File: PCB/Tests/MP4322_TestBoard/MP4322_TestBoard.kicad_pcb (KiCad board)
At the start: 2 copper layers, 30 parts, among them J1 Conn_01x02, J2 Conn_01x02, U7 MP4322GDE-P

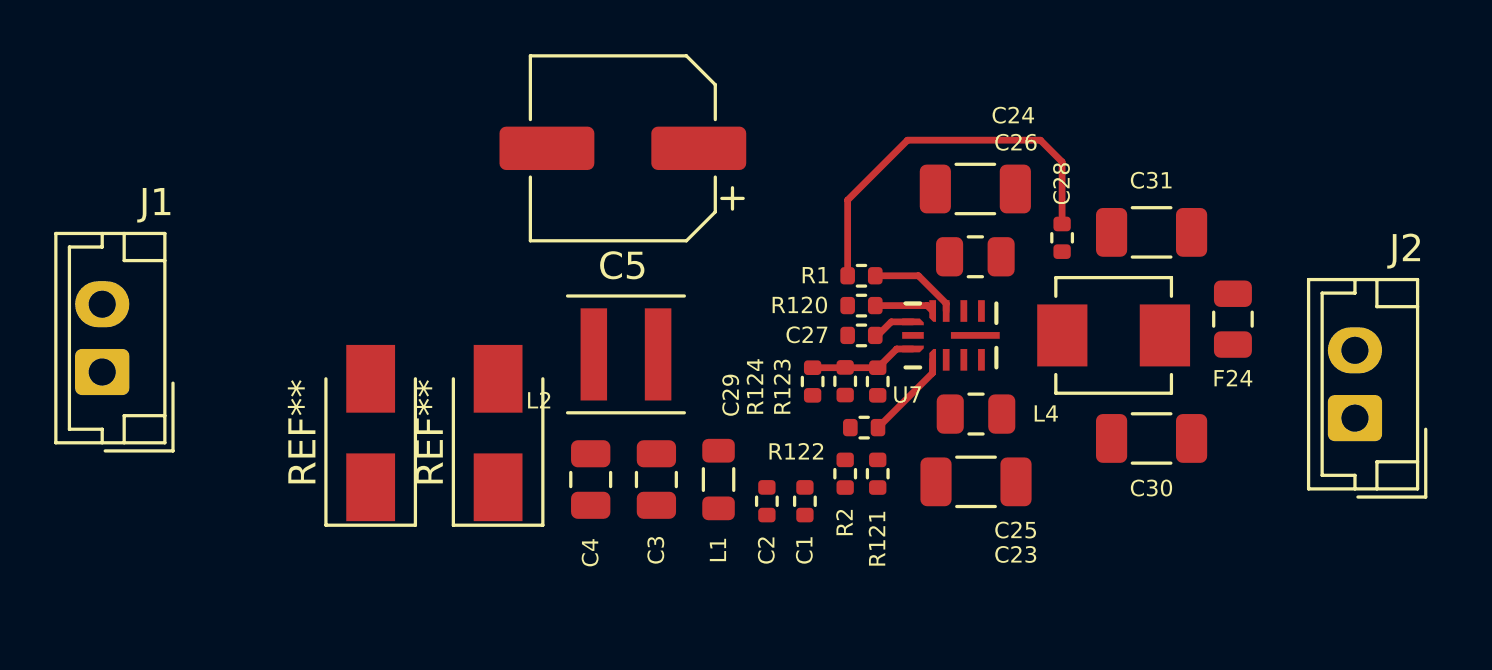
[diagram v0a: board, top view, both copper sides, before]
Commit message: Finished MP4322 evaluation board
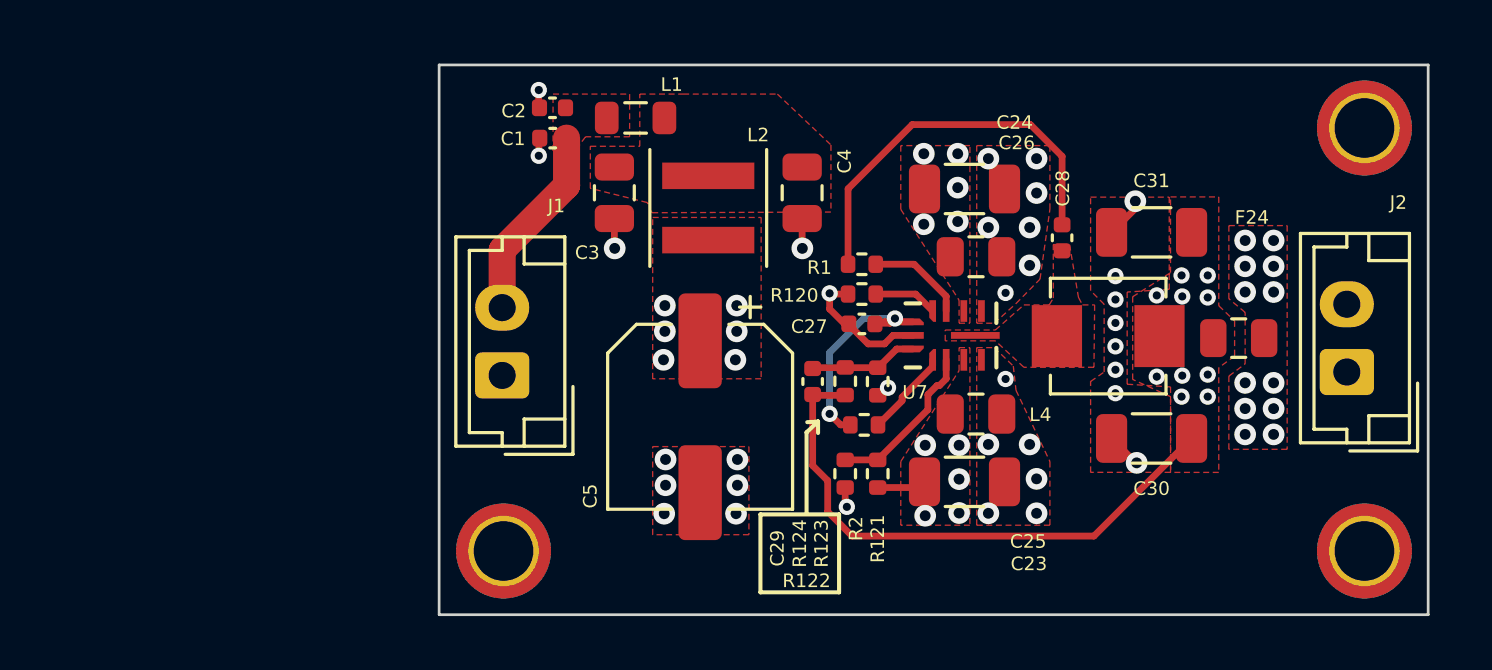
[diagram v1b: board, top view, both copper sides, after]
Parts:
- removed REF** (x2): D_SMA, Diode_SMD:D_SMA
- added H1: MountingHole_Pad, MountingHole:MountingHole_2.2mm_M2_ISO7380_Pad_TopBottom, F.Cu at (126.2, 98.5)
- added H2: MountingHole_Pad, MountingHole:MountingHole_2.2mm_M2_ISO7380_Pad_TopBottom, F.Cu at (126.2, 114.2)
- added H3: MountingHole_Pad, MountingHole:MountingHole_2.2mm_M2_ISO7380_Pad_TopBottom, F.Cu at (94.4, 114.2)
- C1, C2, C27, C28, C29: footprint Resistor_SMD:R_0402_1005Metric -> Capacitor_SMD:C_0402_1005Metric
- F24: value 500mA -> 2A
- moved C2 16.5 mm to (96.2, 97.8), turned to 180 degrees
- moved C1 16.3 mm to (96.2, 98.9), turned to 180 degrees
- moved J1 14.8 mm to (94.3, 107.7)
- moved L1 13.7 mm to (99.3, 98.2), turned to 0 degrees
- moved C4 13.1 mm to (105.4, 100.9)
- moved C3 10.7 mm to (98.5, 100.9)
- moved C5 10.3 mm to (101.7, 109.2), turned to -90 degrees
- moved L2 6.19 mm to (102.0, 101.5), turned to 90 degrees
- moved J2 1.73 mm to (125.5, 107.5)
- moved F24 0.73 mm to (121.5, 106.3), turned to 180 degrees
- moved C27 0.43 mm to (107.6, 105.8)
- moved R1 0.43 mm to (107.6, 103.6)
- moved R120 0.43 mm to (107.6, 104.7)
- moved C23 0.42 mm to (111.4, 111.6)
- moved C24 0.40 mm to (111.4, 100.8)
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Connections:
- net /MP4322/PREFUSE_3V3 renamed /MP4322/PREFUSE
- net Net-(L4-Pad1) renamed /MP4322/PRECOIL
- net Net-(R122-Pad2) renamed /MP4322/PGO
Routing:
- net /MP4322/PREFUSE: track 0.00 -> 21.0 mm, vias 0 -> 10
- net GND: track 0.00 -> 12.6 mm, vias 0 -> 34
- net +12V: track 0.00 -> 6.83 mm
- net Net-(C27-Pad1): track 1.60 -> 8.41 mm, vias 0 -> 2
- net Net-(R121-Pad2): track 0.00 -> 5.99 mm
- net 12V_FILTERED: track 0.00 -> 1.81 mm, vias 0 -> 16
- net +3.3V: vias 0 -> 12
- added copper zone on F.Cu, net +12V
- added copper zone on F.Cu, net +3.3V
- added copper zone on In2.Cu, net +3.3V
- added copper zone on F.Cu, net /MP4322/PRECOIL
- added copper zone on F.Cu, net /MP4322/PREFUSE
- added copper zone on In2.Cu, net /MP4322/PREFUSE
- added copper zone on F.Cu, net 12V_FILTERED
- added copper zone on In2.Cu, net 12V_FILTERED
- added copper zone on F.Cu, net GND
- added copper zone on In1.Cu, net GND
- added copper zone on F.Cu, net Net-(C3-Pad1)
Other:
- board outline added: 36.5 x 20.3 mm
- copper layers 2 -> 4
